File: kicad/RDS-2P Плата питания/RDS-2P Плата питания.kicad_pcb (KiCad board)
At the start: 2 copper layers, 100 x 100 mm, 15 parts, among them J1 XT30U, J2 XT30U2, J3 ЗАР, J4 ВЫКЛ, J5 8.4V, J6 8.4V, J7 5V, J8 ИНД, U1 Converter_Mini560, U2 BMS_2S_20A

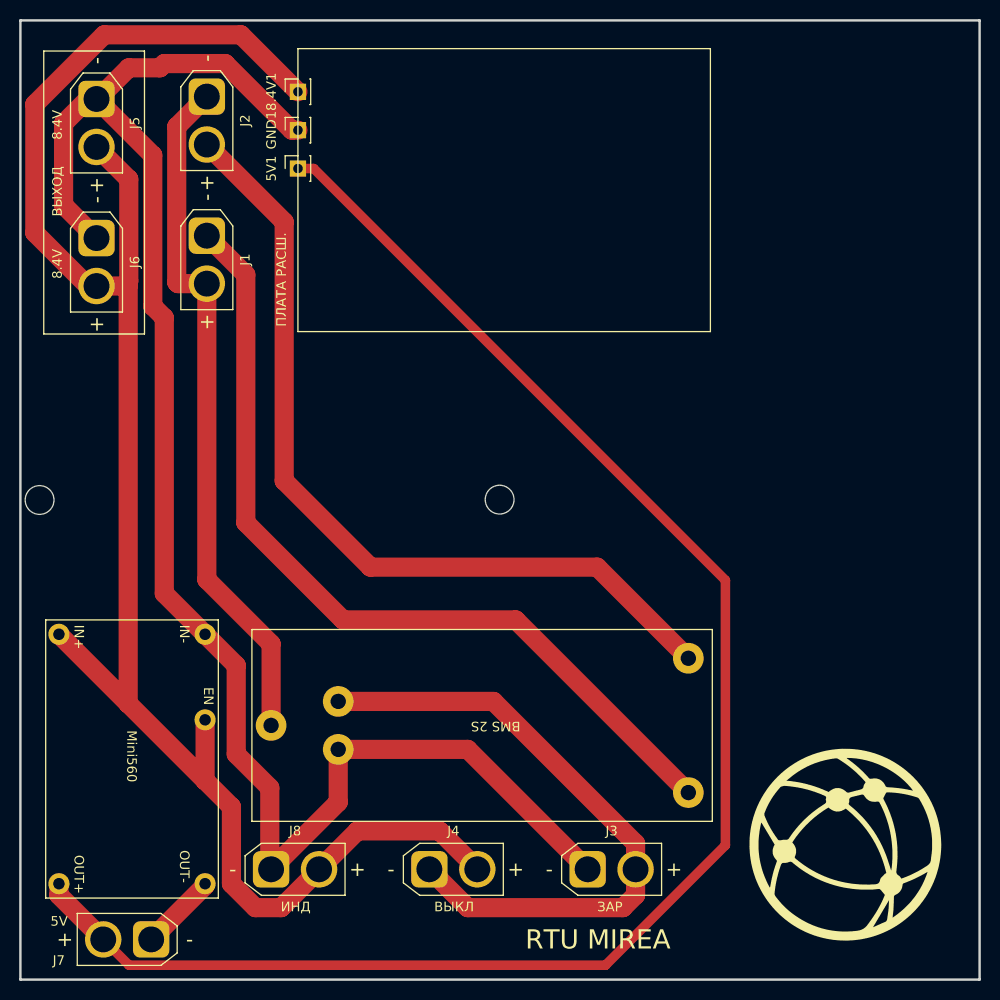
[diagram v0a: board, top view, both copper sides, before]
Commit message: Fix: pinout Mini560
Исправил распиновку Mini560 на платах
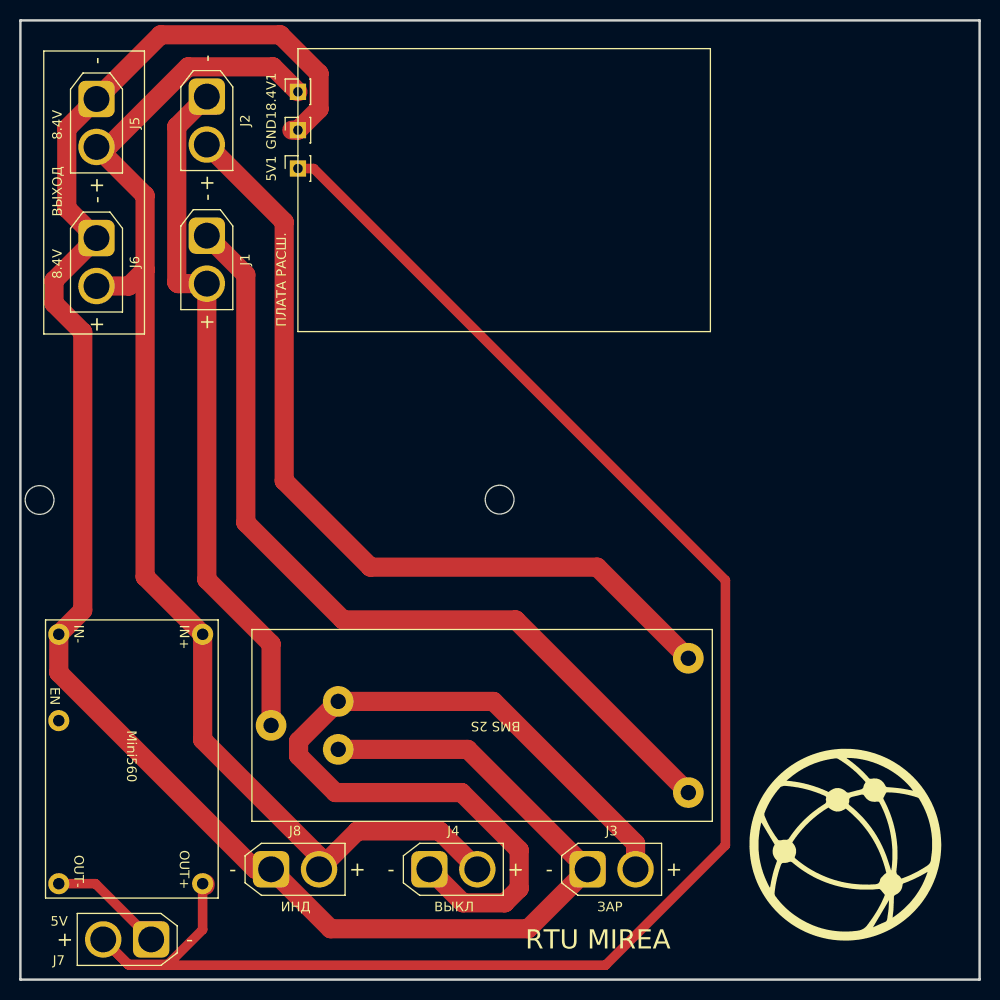
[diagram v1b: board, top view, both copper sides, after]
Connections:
- U1 pad 5: Net-(8.4V1-Pin_1) -> 0
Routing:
- net Net-(8.4V1-Pin_1): track 189.4 -> 137.1 mm
- net Net-(J3-Pad1): track 66.2 -> 89.7 mm
- net Net-(GND1-Pin_1): track 178.3 -> 201.6 mm
- net Net-(5V1-Pin_1): track 169.8 -> 179.4 mm
- net Net-(U1-OUT-): track 8.14 -> 12.6 mm
